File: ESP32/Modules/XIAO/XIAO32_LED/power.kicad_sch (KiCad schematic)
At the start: 2 parts, among them U2 BQ24092DGQR

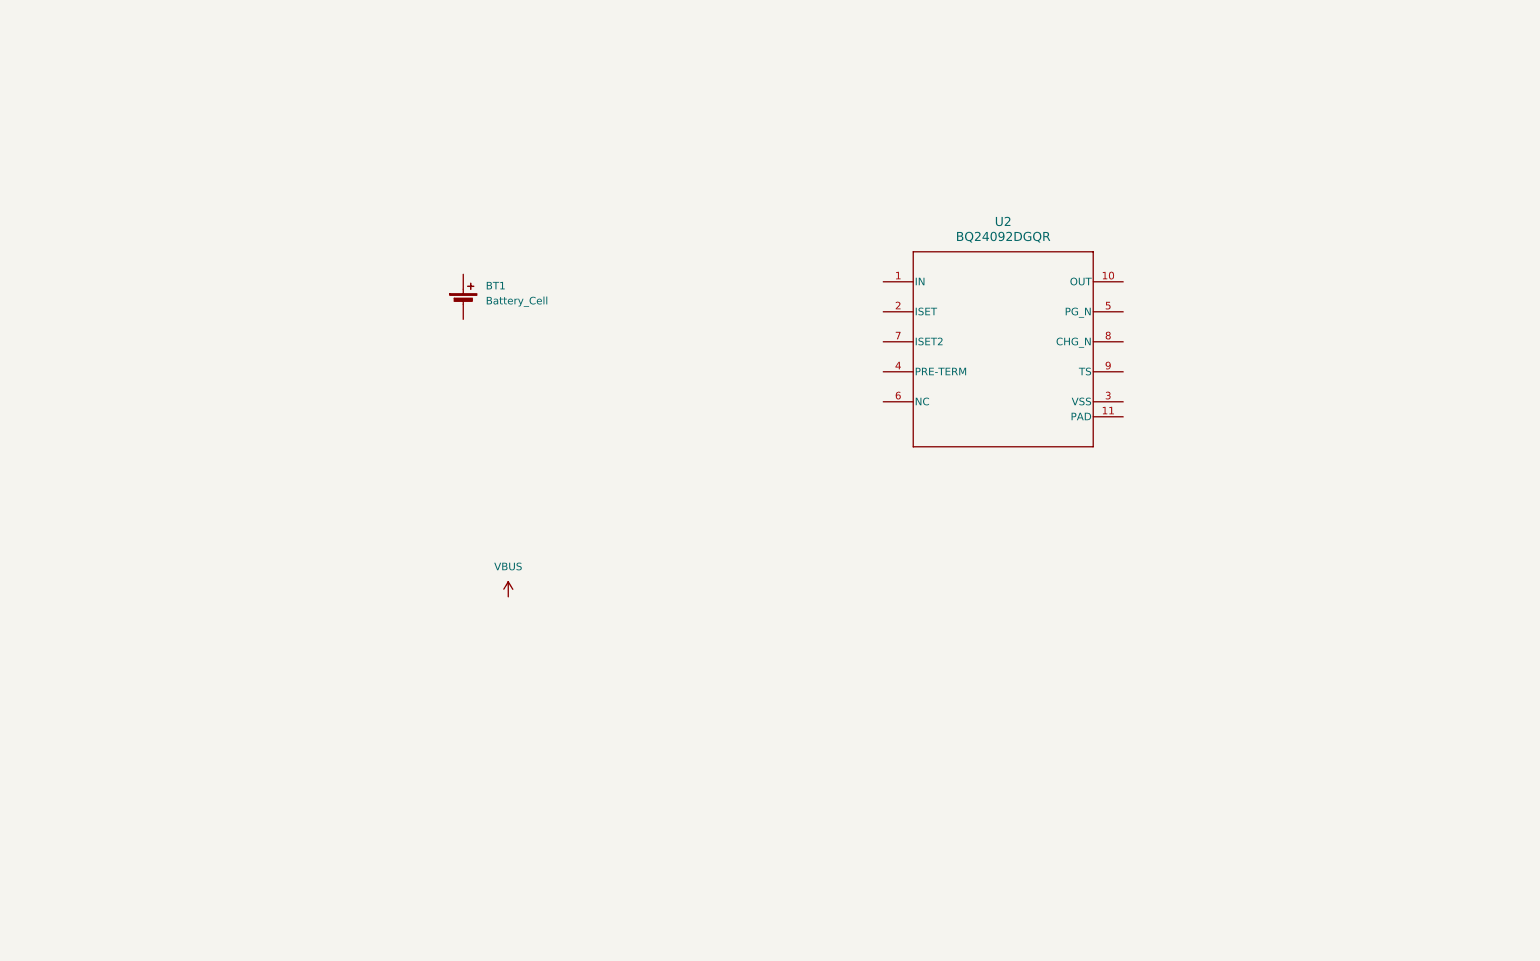
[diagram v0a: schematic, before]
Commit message: Initial wiring of Power and Connectors pages
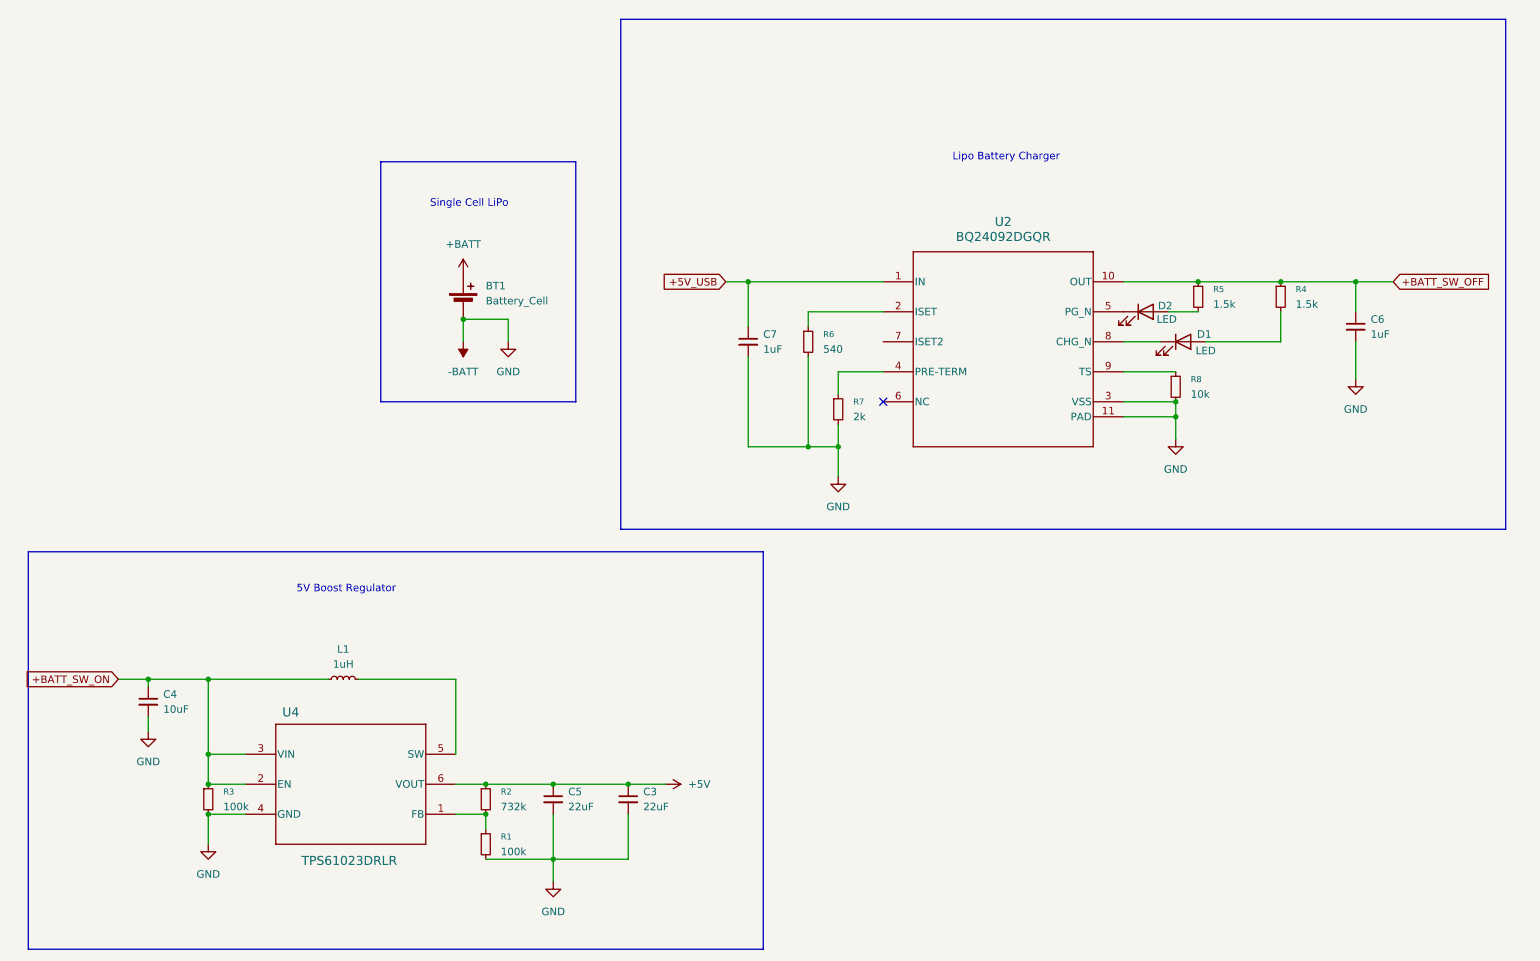
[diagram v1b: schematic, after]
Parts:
- added C3, C5: 22uF, symbol Device:C_Small
- added C4: 10uF, symbol Device:C_Small
- added C6, C7: 1uF, symbol Device:C_Small
- added D1, D2: LED, symbol Device:LED
- added L1: 1uH, symbol Device:L_Small
- added R1, R3: 100k, symbol Device:R_Small
- added R2: 732k, symbol Device:R_Small
- added R4, R5: 1.5k, symbol Device:R_Small
- added R6: 540, symbol Device:R_Small
- added R7: 2k, symbol Device:R_Small
- added R8: 10k, symbol Device:R_Small
- added U4: TPS61023DRLR, DRL0006A, symbol My_Converter_DCDC:TPS61023DRLR
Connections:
- net +BATT: now reaches BT1.1 (+)
- net -BATT: now reaches BT1.2 (-)
- net -BATT: now also U2.11 (PAD), U2.3 (VSS), C3.2, C4.2, C5.2, C6.2, C7.2, R1.2, R3.2, R6.2, R7.2, R8.2, U4.4 (GND)
- net +5V_USB: now reaches U2.1 (IN)
- net +5V_USB: now also C7.1
- net +BATT_SW_OFF: now reaches U2.10 (OUT)
- net +BATT_SW_OFF: now also C6.1, R4.1, R5.1
- net at U2.2 (ISET): now also R6.1
- net at U2.4 (PRE-TERM): now also R7.1
- net at U2.5 (PG_N): now also D2.1 (K)
- net at U2.8 (CHG_N): now also D1.1 (K)
- net at U2.9 (TS): now also R8.1
- new net: D1.2 (A), R4.2
- new net: R1.1, R2.2, U4.1 (FB)
- new net: L1.2, U4.5 (SW)
- new net: D2.2 (A), R5.2
- new net +5V: C3.1, C5.1, R2.1, U4.6 (VOUT)
- new net +BATT_SW_ON: C4.1, L1.1, R3.1, U4.2 (EN), U4.3 (VIN)
- no-connect marks 0 -> 1
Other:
- note added: "5V Boost Regulator"
- note added: "Lipo Battery Charger"
- note added: "Single Cell LiPo"

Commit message: XIAO32_LED: MCU wired up
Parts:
- added SW1: SW_SPDT, symbol Switch:SW_SPDT
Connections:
- net +5V: no longer R2.1
- net +5V_USB: no longer U2.1 (IN)
- net +BATT: now also SW1.2 (B)
- net +BATT_SW_ON: now also SW1.1 (A); no longer L1.1, R3.1
- net -BATT: now also C6.1, SW1.3 (C); no longer R1.2, R3.2, R6.2, R7.2, R8.2, U2.11 (PAD), U2.3 (VSS)
- net at D1.2 (ISET): no longer R4.2
- net at U4.5 (SW): no longer L1.2
- net at D2.1 (IN): no longer U2.5 (PG_N)
- net at D1.1 (IN): no longer U2.8 (CHG_N)
- net at D2.2 (ISET): no longer R5.2
- removed net +BATT_SW_OFF: C6.1, R4.1, R5.1, U2.10 (OUT)
- now unconnected: U4.1 (FB)
- no-connect marks 1 -> 2
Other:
- moved on the sheet: BT1, C3, C4, C6, U4
